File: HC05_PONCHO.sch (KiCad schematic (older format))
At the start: 34 parts, among them J1 MOUNT_HOLE, J2 MOUNT_HOLE, J3 BARREL_JACK, Q1 Q_NPN_EBC, SW1 SW_SPDT, SW2 SW_Push, SW3 SW_Push, U1 LD1117S33CTR, U2 MOUDLE-BLUETOOTH-HC-05(34P-27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, U3 HMC5883L

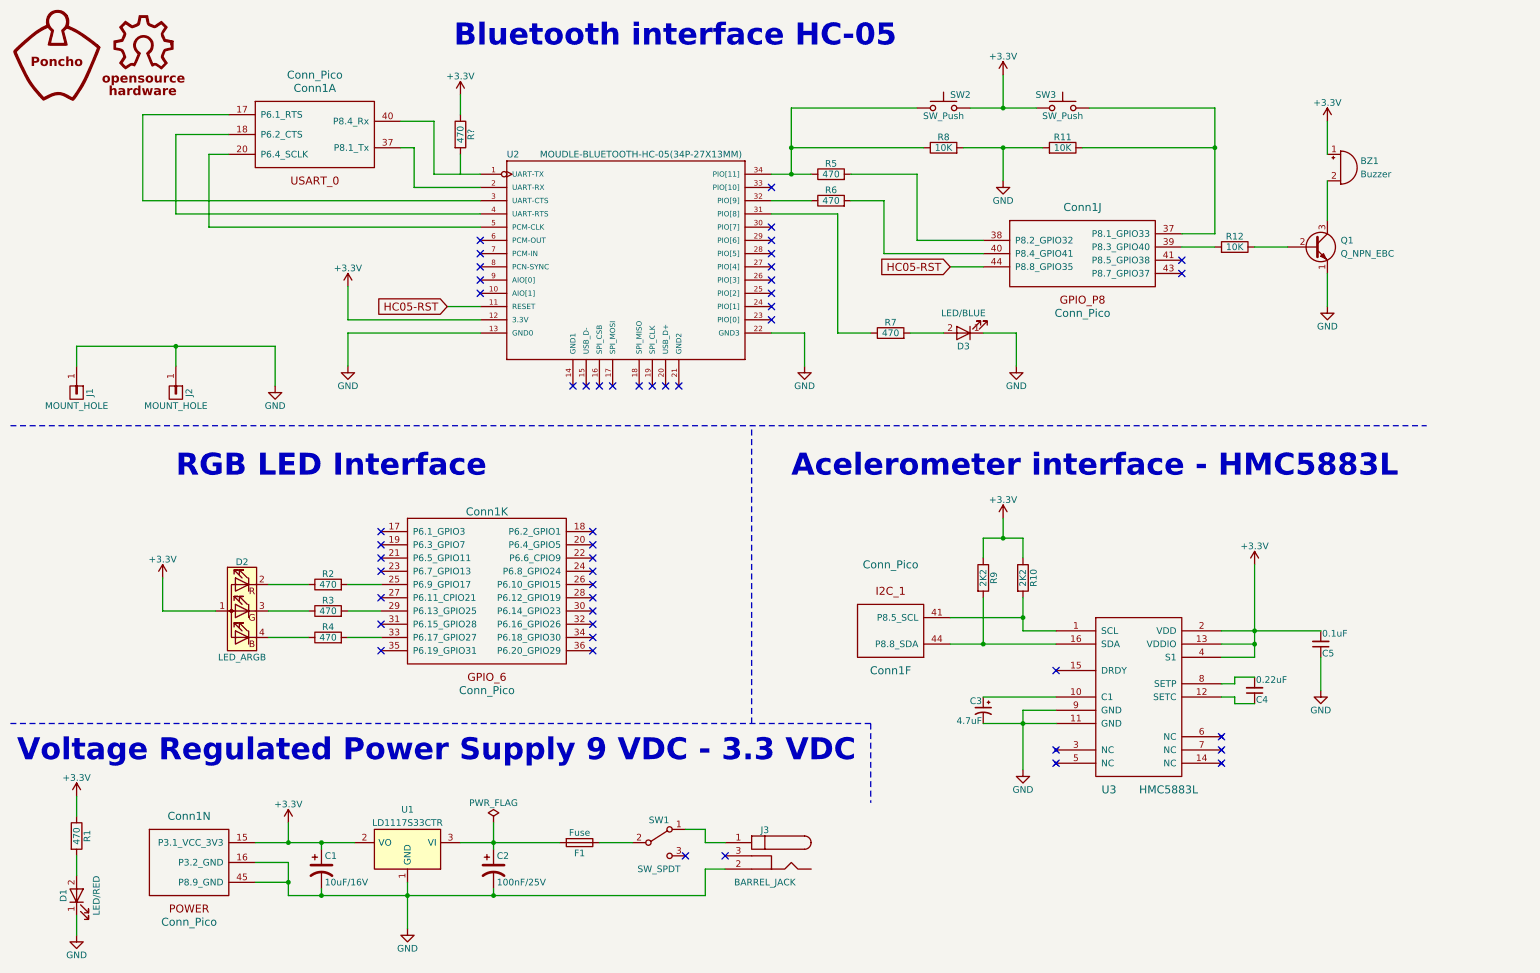
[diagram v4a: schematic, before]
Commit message: Avance para segunda revision.
Se realizan todos los cambios solicitados por el docente y el corrector, ademas se continua con el avance hasta el placement del PCB
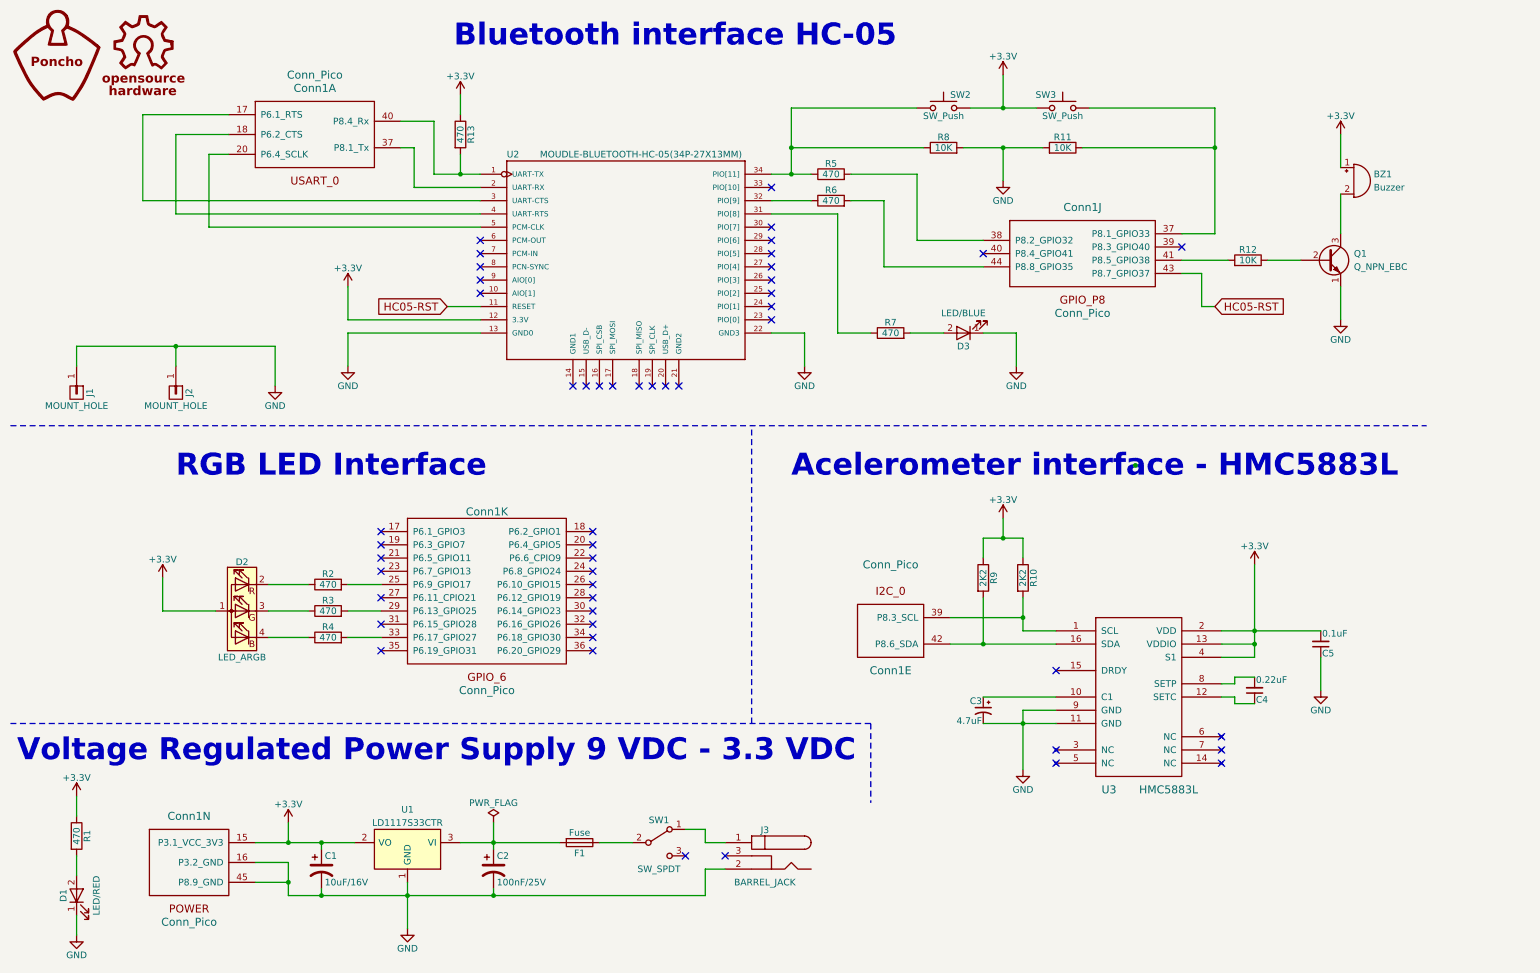
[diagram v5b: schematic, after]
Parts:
- removed unit 6 of Conn1
- added unit 5 of Conn1
- C3: footprint Capacitors_Tantalum_SMD:CP_Tantalum_Case-A_EIA-3216-18_Hand -> Capacitors_SMD:C_0402
- C4, C5: footprint Capacitors_SMD:C_1206_HandSoldering -> Capacitors_SMD:C_0201
- D1, D3: footprint LEDs:LED_1206 -> LEDs:LED_0805_HandSoldering
- J1, J2: footprint Mounting_Holes:MountingHole_3mm_Pad_Via -> Mounting_Holes:MountingHole_2.5mm_Pad_Via
- R1, R11, R12, R2, R3, R4, R5, R6, R7, R8: footprint Resistors_SMD:R_0603_HandSoldering -> Resistors_SMD:R_0805_HandSoldering
- R10, R9: footprint Resistors_SMD:R_0603_HandSoldering -> Resistors_SMD:R_0402
- R13: renamed from R?; footprint Resistors_SMD:R_0603_HandSoldering -> Resistors_SMD:R_0805_HandSoldering
- SW2, SW3: footprint Buttons_Switches_THT:SW_PUSH_6mm -> Buttons_Switches_SMD:SW_SPST_EVQPE1
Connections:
- net HC05-RST: now also Conn1.43 (P8.7_GPIO37); no longer Conn1.44 (P8.8_GPIO35)
- net at R10.2, U3.1 (SCL): now also Conn1.39 (P8.3_SCL)
- net at R9.2, U3.16 (SDA): now also Conn1.42 (P8.6_SDA)
- net at Conn1.40 (P8.4_Rx), U2.1 (UART-TX): now also R13.2
- net at Conn1.39 (P8.3_GPIO40): no longer R12.2
- net at Conn1.40 (P8.4_GPIO41): no longer R6.2
- net at Conn1.41 (P8.5_GPIO38): now also R12.2
- new net: Conn1.44 (P8.8_GPIO35), R6.2
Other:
- moved on the sheet: BZ1, Q1, R12

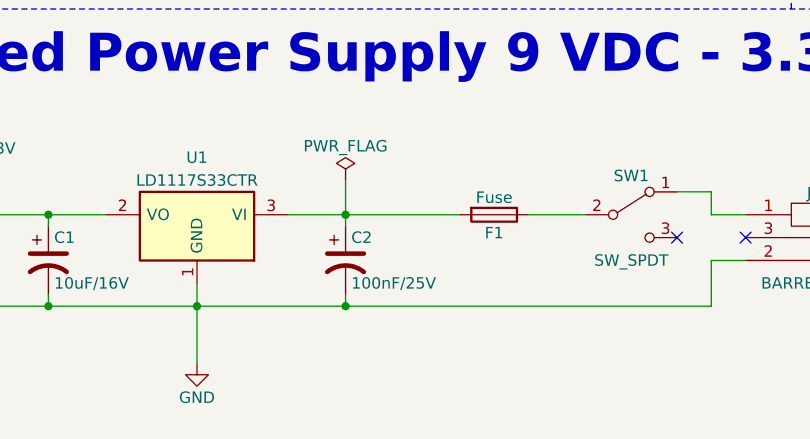
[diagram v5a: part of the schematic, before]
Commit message: Revision de carpetas
Limpieza de documentos que ya no se utilizaban en el proyecto.
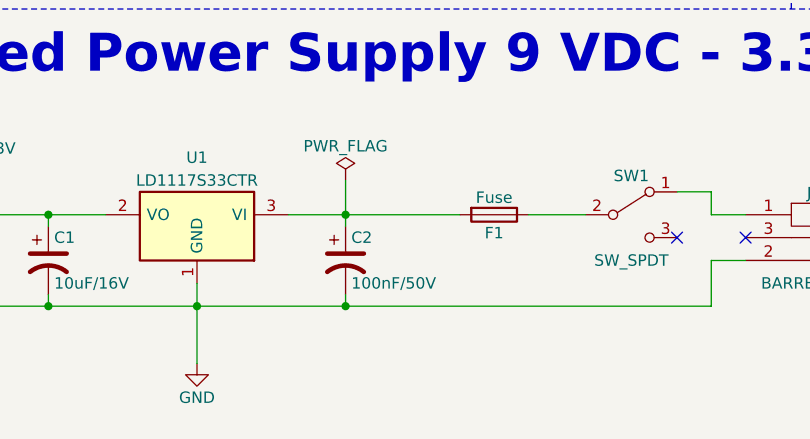
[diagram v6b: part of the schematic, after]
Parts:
- BZ1: footprint Buzzers_Beepers:MagneticBuzzer_Kingstate_KCG0601 -> HC05_PONCHO:MagneticBuzzer_Kingstate_KCG0601
- C1: footprint Capacitors_SMD:CP_Elec_3x5.3 -> HC05_PONCHO:CP_Elec_3x5.3; Desc (none) -> CAP ALUM 10UF 20% 16V SMD; Digikey# (none) -> PCE3878CT-ND; Manf (none) -> Panasonic Electronic Components; Manf# (none) -> EEE-1CA100SR
- C2: value 100nF/25V -> 100nF/50V; footprint Capacitors_SMD:CP_Elec_3x5.3 -> HC05_PONCHO:CP_Elec_3x5.3; Desc (none) -> CAP 0.10 UF 20% 50 V; Digikey# (none) -> 732-8266-1-ND; Manf (none) -> Wurth Electronics Inc.; Manf# (none) -> 865230640001
- C3: footprint Capacitors_SMD:C_0402 -> HC05_PONCHO:C_0402; Desc (none) -> CAP CER 4.7UF 6.3V X5R 0402; Digikey# (none) -> 490-5915-1-ND; Manf (none) -> Murata Electronics North America; Manf# (none) -> GRM155R60J475ME47D
- C4: footprint Capacitors_SMD:C_0201 -> HC05_PONCHO:C_0201; Desc (none) -> CAP CER 0.22UF 6.3V X6S 0201; Digikey# (none) -> 490-10392-1-ND; Manf (none) -> Murata Electronics North America; Manf# (none) -> GRM033C80J224KE90D
- C5: footprint Capacitors_SMD:C_0201 -> HC05_PONCHO:C_0201; Desc (none) -> CAP CER 0.1UF 6.3V X5R 0201; Digikey# (none) -> 490-3167-2-ND; Manf (none) -> Murata Electronics North America; Manf# (none) -> GRM033R60J104KE19D
- Conn1: footprint pico_ciaa_ponchos:Conn_Pico_Ciaa -> HC05_PONCHO:Conn_Pico_Ciaa
- Conn1: footprint (none) -> HC05_PONCHO:Conn_Pico_Ciaa
- D1, D3: footprint LEDs:LED_0805_HandSoldering -> HC05_PONCHO:LED_0805_HandSoldering
- D2: footprint SML-LX0404SIUPGUSB:DIOC0404X01-4N -> HC05_PONCHO:DIOC0404X01-4N
- F1: footprint Fuse_Holders_and_Fuses:Fuse_SMD2920 -> HC05_PONCHO:Fuse_SMD2920
- J1, J2: footprint Mounting_Holes:MountingHole_2.5mm_Pad_Via -> HC05_PONCHO:MountingHole_2.5mm_Pad_Via
- J3: footprint Connectors:BARREL_JACK -> HC05_PONCHO:BARREL_JACK
- Q1: footprint TO_SOT_Packages_SMD:SOT-23 -> HC05_PONCHO:SOT-23
- R1: footprint Resistors_SMD:R_0805_HandSoldering -> HC05_PONCHO:R_0805_HandSoldering; Desc (none) -> RES SMD 470 OHM 5% 1/8W 0805; Digikey# (none) -> 1276-5523-2-ND; Manf (none) -> Samsung Electro-Mechanics America, Inc; Manf# (none) -> RC2012J471CS
- R10, R9: footprint Resistors_SMD:R_0402 -> HC05_PONCHO:R_0402; Desc (none) -> RES SMD 2.2K OHM 5% 1/8W 0805; Digikey# (none) -> 1276-5537-2-ND; Manf (none) -> Samsung Electro-Mechanics America, Inc; Manf# (none) -> RC2012J222CS
- R11, R8: footprint Resistors_SMD:R_0805_HandSoldering -> HC05_PONCHO:R_0805_HandSoldering; Desc (none) -> RES SMD 10K OHM 5% 1/8W 0805; Digikey# (none) -> 1276-5552-2-ND; Manf (none) -> Samsung Electro-Mechanics America, Inc; Manf# (none) -> RC2012J103CS
- R12: footprint Resistors_SMD:R_0805_HandSoldering -> HC05_PONCHO:R_0805_HandSoldering; Desc (none) -> RES SMD 10K OHM 5% 1/8W 0805; Digikey# (none) -> 1277-5552-2-ND; Manf (none) -> Samsung Electro-Mechanics America, Inc; Manf# (none) -> RC2012J103CS
- R13: footprint Resistors_SMD:R_0805_HandSoldering -> HC05_PONCHO:R_0805_HandSoldering; Desc (none) -> RES SMD 470 OHM 5% 1/8W 0805; Digikey# (none) -> 1278-5523-2-ND; Manf (none) -> Samsung Electro-Mechanics America, Inc; Manf# (none) -> RC2012J471CS
- R2: footprint Resistors_SMD:R_0805_HandSoldering -> HC05_PONCHO:R_0805_HandSoldering; Desc (none) -> RES SMD 470 OHM 5% 1/8W 0805; Digikey# (none) -> 1279-5523-2-ND; Manf (none) -> Samsung Electro-Mechanics America, Inc; Manf# (none) -> RC2012J471CS
- R3: footprint Resistors_SMD:R_0805_HandSoldering -> HC05_PONCHO:R_0805_HandSoldering; Desc (none) -> RES SMD 470 OHM 5% 1/8W 0805; Digikey# (none) -> 1280-5523-2-ND; Manf (none) -> Samsung Electro-Mechanics America, Inc; Manf# (none) -> RC2012J471CS
- R4: footprint Resistors_SMD:R_0805_HandSoldering -> HC05_PONCHO:R_0805_HandSoldering; Desc (none) -> RES SMD 470 OHM 5% 1/8W 0805; Digikey# (none) -> 1281-5523-2-ND; Manf (none) -> Samsung Electro-Mechanics America, Inc; Manf# (none) -> RC2012J471CS
- R5: footprint Resistors_SMD:R_0805_HandSoldering -> HC05_PONCHO:R_0805_HandSoldering; Desc (none) -> RES SMD 470 OHM 5% 1/8W 0805; Digikey# (none) -> 1282-5523-2-ND; Manf (none) -> Samsung Electro-Mechanics America, Inc; Manf# (none) -> RC2012J471CS
- R6: footprint Resistors_SMD:R_0805_HandSoldering -> HC05_PONCHO:R_0805_HandSoldering; Desc (none) -> RES SMD 470 OHM 5% 1/8W 0805; Digikey# (none) -> 1283-5523-2-ND; Manf (none) -> Samsung Electro-Mechanics America, Inc; Manf# (none) -> RC2012J471CS
- R7: footprint Resistors_SMD:R_0805_HandSoldering -> HC05_PONCHO:R_0805_HandSoldering; Desc (none) -> RES SMD 470 OHM 5% 1/8W 0805; Digikey# (none) -> 1284-5523-2-ND; Manf (none) -> Samsung Electro-Mechanics America, Inc; Manf# (none) -> RC2012J471CS
- SW1: footprint Buttons_Switches_THT:SW_NKK_G1xJP -> HC05_PONCHO:SW_NKK_G1xJP
- SW2, SW3: footprint Buttons_Switches_SMD:SW_SPST_EVQPE1 -> HC05_PONCHO:SW_SPST_EVQPE1
- U1: footprint TO_SOT_Packages_SMD:SOT-223 -> HC05_PONCHO:SOT-223
- U2: footprint MOUDLE-BLUETOOTH-HC-05_34P-27X13MM_:BT34P-SMD-1.5-26.9X13.0X2.2MM -> HC05_PONCHO:BT34P-SMD-1.5-26.9X13.0X2.2MM; Desc (none) -> Unavailable; Digikey# (none) -> None; Manf (none) -> HC-05; Mouser# (none) -> None
- U3: footprint HMC5883L:LPCC-16 -> HC05_PONCHO:LPCC-16
